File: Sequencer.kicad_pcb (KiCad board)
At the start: 2 copper layers, 100.6 x 100 mm, 230 parts, among them J1 Conn_02x03_Odd_Even, J2 Conn_02x05_Odd_Even, J3 Conn_02x03_Odd_Even, J4 Conn_01x03, Q1 BC847, Q2 BC847, Q3 BC847, Q4 BC847, SW1 SW_Push, SW10 SW_SPDT_MSM, SW11 SW_SPDT_MSM, SW12 SW_SPDT_MSM, SW2 SW_SPDT_MSM, SW3 SW_SPDT_MSM, SW4 SW_SPDT_MSM, SW5 SW_SPDT_MSM, SW6 SW_SPDT_MSM, SW7 SW_SPDT, SW8 SW_SPDT, SW9 SW_SPDT_MSM, U1 L7805, U10 TL072, U11 74AHCT1G125, U12 TL072, U13 74AHCT1G125, U14 TL072, U2 ATmega328PB-AU, U3 74AHCT1G125, U4 MCP6002-xMS, U5 MCP6002-xMS, U6 MCP6002-xMS, U7 MCP6002-xMS, U8 TL072, U9 74AHCT1G125, X1 20MHz

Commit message: Power section placement.
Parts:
- moved D3 82.6 mm to (107.9, 76.3), turned to 180 degrees
- moved R3 79.5 mm to (107.7, 79.6), turned to 180 degrees
- moved C5 41.2 mm to (128.2, 76.8)
- moved R15 28.4 mm to (158.9, 82.1), turned to 180 degrees
- moved C3 26.4 mm to (158.9, 72.2), turned to 0 degrees
- moved C4 24.6 mm to (158.9, 76.8), turned to 0 degrees
- moved C1 21.9 mm to (168.8, 76.8)
- moved U1 20.6 mm to (148.5, 74.5)
- moved D8 16.7 mm to (162.7, 59.0)
- moved C7 14.4 mm to (154.6, 120.2), turned to 0 degrees
- moved R13 12.9 mm to (158.9, 67.7)
- moved C2 12.6 mm to (189.1, 76.8)
- moved R14 11.8 mm to (158.9, 63.1)
- moved R4 10.4 mm to (142.1, 120.0), turned to 0 degrees
- moved R19 8.19 mm to (133.3, 114.4)
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
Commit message: PWM pin swap.
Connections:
- C1 pad 2: (no net) -> GND
- C10 pad 2: (no net) -> GND
- C12 pad 2: (no net) -> GND
- C13 pad 2: (no net) -> GND
- C15 pad 2: (no net) -> GND
- C16 pad 2: (no net) -> GND
- C18 pad 2: (no net) -> GND
- C19 pad 2: (no net) -> GND
- C2 pad 1: (no net) -> GND
- C21 pad 2: (no net) -> GND
- C22 pad 1: (no net) -> GND
- C23 pad 2: (no net) -> GND
- C24 pad 2: (no net) -> GND
- C25 pad 2: (no net) -> GND
- C26 pad 2: (no net) -> GND
- C29 pad 2: (no net) -> GND
- C3 pad 2: (no net) -> GND
- C30 pad 1: (no net) -> GND
- C31 pad 2: (no net) -> GND
- C32 pad 2: (no net) -> GND
- C33 pad 2: (no net) -> GND
- C34 pad 2: (no net) -> GND
- C37 pad 2: (no net) -> GND
- C38 pad 1: (no net) -> GND
- C39 pad 2: (no net) -> GND
- C4 pad 2: (no net) -> GND
- C40 pad 2: (no net) -> GND
- C41 pad 2: (no net) -> GND
- C42 pad 2: (no net) -> GND
- C45 pad 2: (no net) -> GND
- C46 pad 1: (no net) -> GND
- C47 pad 2: (no net) -> GND
- C48 pad 2: (no net) -> GND
- C49 pad 2: (no net) -> GND
- C5 pad 2: (no net) -> GND
- C50 pad 2: (no net) -> GND
- C6 pad 1: (no net) -> GND
- C7 pad 2: (no net) -> GND
- C8 pad 1: (no net) -> GND
- C9 pad 2: (no net) -> GND
- D13 pad 1: (no net) -> GND
- D14 pad 1: (no net) -> GND
- D15 pad 1: (no net) -> GND
- D3 pad 1: (no net) -> GND
- D4 pad 1: (no net) -> GND
- D5 pad 1: (no net) -> GND
- J-Inv1 pad S: (no net) -> GND
- J-Inv10 pad S: (no net) -> GND
- J-Inv11 pad S: (no net) -> GND
- J-Inv12 pad S: (no net) -> GND
- J-Inv13 pad S: (no net) -> GND
- J-Inv14 pad S: (no net) -> GND
- J-Inv15 pad S: (no net) -> GND
- J-Inv16 pad S: (no net) -> GND
- J-Inv2 pad S: (no net) -> GND
- J-Inv2 pad TN: (no net) -> GND
- J-Inv3 pad S: (no net) -> GND
- J-Inv4 pad S: (no net) -> GND
- J-Inv5 pad S: (no net) -> GND
- J-Inv5 pad TN: (no net) -> GND
- J-Inv6 pad S: (no net) -> GND
- J-Inv7 pad S: (no net) -> GND
- J-Inv8 pad S: (no net) -> GND
- J-Inv9 pad S: (no net) -> GND
- J1 pad 1: (no net) -> GND
- J1 pad 2: (no net) -> GND
- J2 pad 3: (no net) -> GND
- J2 pad 4: (no net) -> GND
- J2 pad 5: (no net) -> GND
- J2 pad 6: (no net) -> GND
- J2 pad 7: (no net) -> GND
- J2 pad 8: (no net) -> GND
- J3 pad 6: (no net) -> GND
- J4 pad 1: (no net) -> GND
- J4 pad 3: CV3 -> CV0
- Q1 pad 2: (no net) -> GND
- Q2 pad 2: (no net) -> GND
- Q3 pad 2: (no net) -> GND
- Q4 pad 2: (no net) -> GND
- R101 pad 2: (no net) -> GND
- R103 pad 2: (no net) -> GND
- R105 pad 1: (no net) -> GND
- R107 pad 2: (no net) -> GND
- R11 pad 2: (no net) -> GND
- R19 pad 2: (no net) -> GND
- R24 pad 2: (no net) -> GND
- R29 pad 2: (no net) -> GND
- R44 pad 1: (no net) -> GND
- R47 pad 2: (no net) -> GND
- R49 pad 2: (no net) -> GND
- R51 pad 1: (no net) -> GND
- R53 pad 2: (no net) -> GND
- R62 pad 1: (no net) -> GND
- R65 pad 2: (no net) -> GND
- R67 pad 2: (no net) -> GND
- R69 pad 1: (no net) -> GND
- R71 pad 2: (no net) -> GND
- R80 pad 1: (no net) -> GND
- R83 pad 2: (no net) -> GND
- R85 pad 2: (no net) -> GND
- R87 pad 1: (no net) -> GND
- R89 pad 2: (no net) -> GND
- R98 pad 1: (no net) -> GND
- RV1 pad 3: (no net) -> GND
- RV2 pad 3: (no net) -> GND
- RV3 pad 3: (no net) -> GND
- RV4 pad 3: (no net) -> GND
- SW1 pad 2: (no net) -> GND
- U1 pad 2: (no net) -> GND
- U11 pad 1: (no net) -> GND
- U11 pad 3: (no net) -> GND
- U13 pad 1: (no net) -> GND
- U13 pad 3: (no net) -> GND
- U2 pad 13: CV0 -> CV2
- U2 pad 14: CV1 -> CV3
- U2 pad 21: (no net) -> GND
- U2 pad 30: CV3 -> CV0
- U2 pad 32: CV2 -> CV1
- U2 pad 5: (no net) -> GND
- U3 pad 1: (no net) -> GND
- U3 pad 3: (no net) -> GND
- U4 pad 4: (no net) -> GND
- U5 pad 4: (no net) -> GND
- U6 pad 4: (no net) -> GND
- U7 pad 4: (no net) -> GND
- U9 pad 1: (no net) -> GND
- U9 pad 3: (no net) -> GND
- X1 pad 2: (no net) -> GND

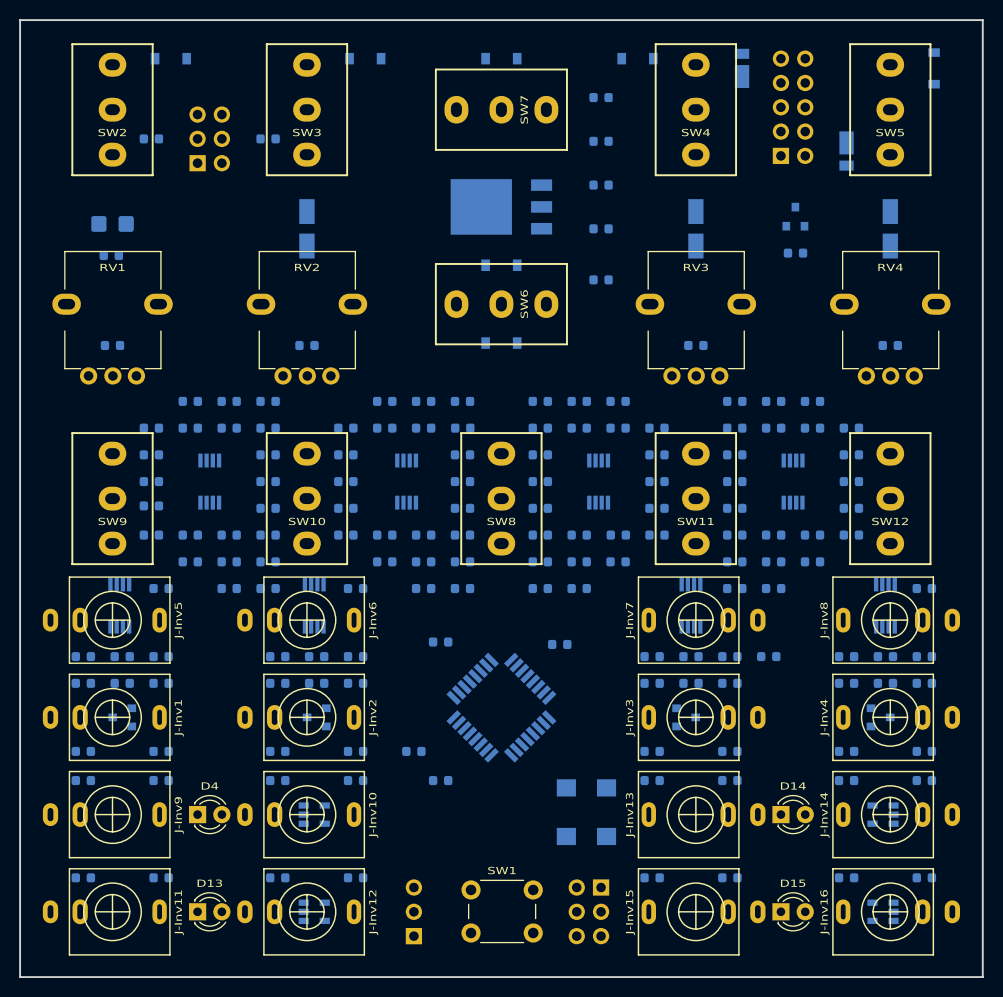
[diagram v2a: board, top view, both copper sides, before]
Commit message: Handrouted power and I2C.
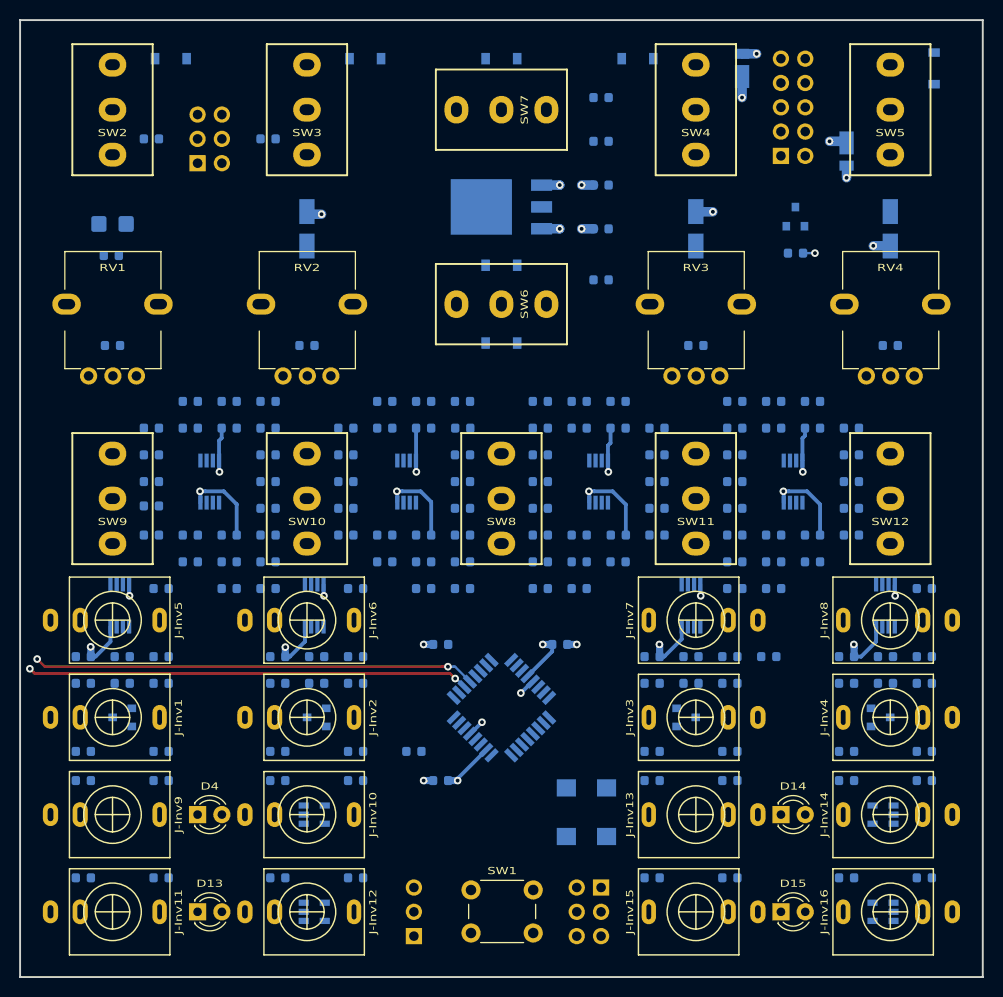
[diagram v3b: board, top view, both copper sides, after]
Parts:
- moved R4 0.25 mm to (142.1, 120.2)
- turned C22 to 180 degrees
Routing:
- net +12V: track 0.00 -> 220.4 mm, vias 0 -> 8
- net +5V: track 0.00 -> 193.6 mm, vias 0 -> 10
- net -12V: track 0.00 -> 139.1 mm, vias 0 -> 7
- net SCL: track 0.00 -> 119.6 mm, vias 0 -> 2
- net SDA: track 0.00 -> 112.9 mm, vias 0 -> 2
- net GND: track 0.00 -> 10.3 mm, vias 0 -> 8
- net Net-(D2-Pad1): track 0.00 -> 7.56 mm, vias 0 -> 1
- net Net-(D1-Pad2): track 0.00 -> 6.81 mm, vias 0 -> 1
- added copper zone on In2.Cu, net +5V
- added copper zone on In1.Cu, net GND
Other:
- copper layers 2 -> 4

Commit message: Autorouted remaining traces.
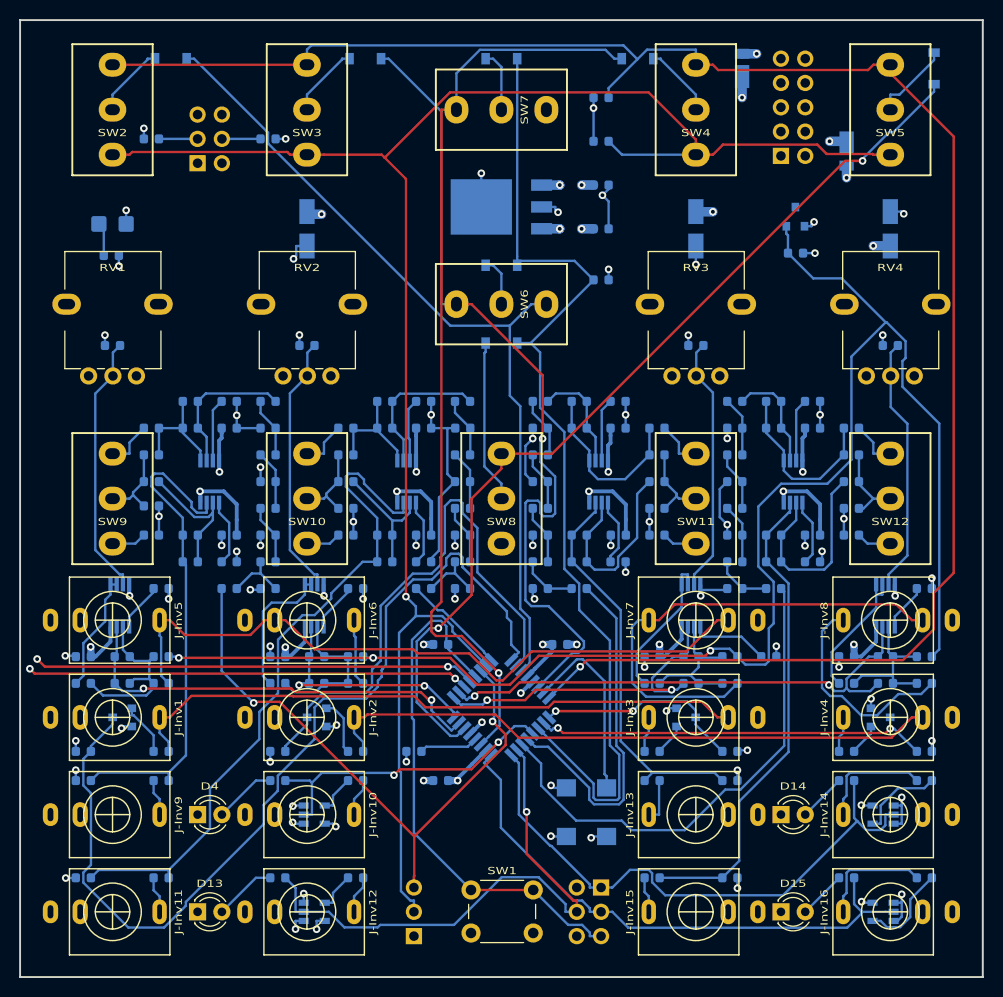
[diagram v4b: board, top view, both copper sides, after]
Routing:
- net Sense1: track 0.00 -> 197.5 mm, vias 0 -> 1
- net Sense0: track 0.00 -> 190.2 mm, vias 0 -> 1
- net VRef-10: track 0.00 -> 166.0 mm, vias 0 -> 3
- net GND: track 10.3 -> 143.3 mm, vias 8 -> 69
- net Sense2: track 0.00 -> 105.0 mm
- net CLK0: track 0.00 -> 99.7 mm
- net Scan3: track 0.00 -> 98.7 mm, vias 0 -> 2
- net Scan2: track 0.00 -> 96.2 mm, vias 0 -> 1
- net Scan0: track 0.00 -> 88.0 mm
- net Scan1: track 0.00 -> 87.3 mm, vias 0 -> 1
- net /CVIn/In: track 0.00 -> 73.0 mm
- net Net-(C36-Pad1): track 0.00 -> 71.5 mm
- net /DigitalIn/In: track 0.00 -> 65.7 mm
- net /sheet5C188821/In: track 0.00 -> 65.4 mm
- net CV0: track 0.00 -> 63.8 mm, vias 0 -> 2
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
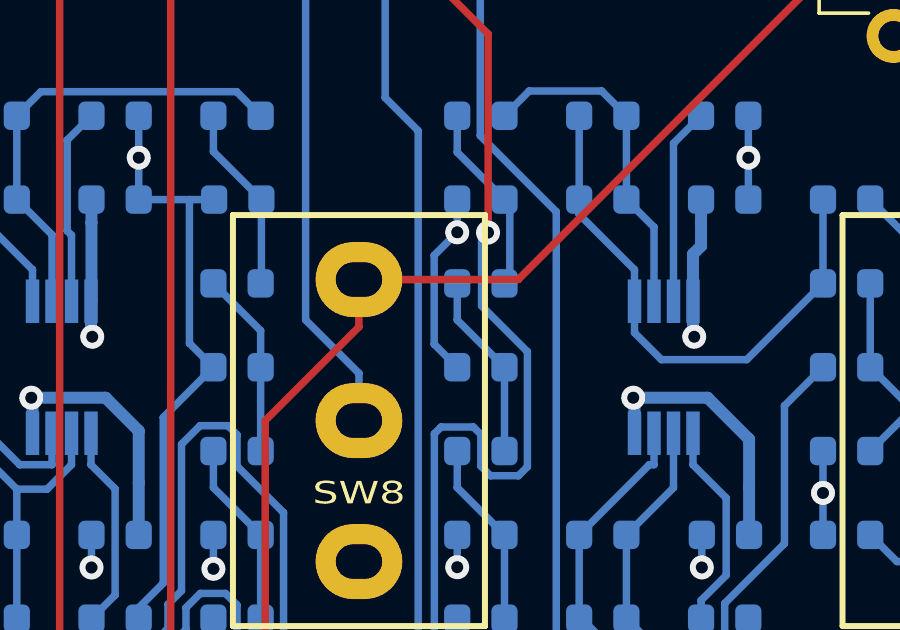
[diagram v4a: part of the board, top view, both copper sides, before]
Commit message: Corrected one single DRC (unconnected).
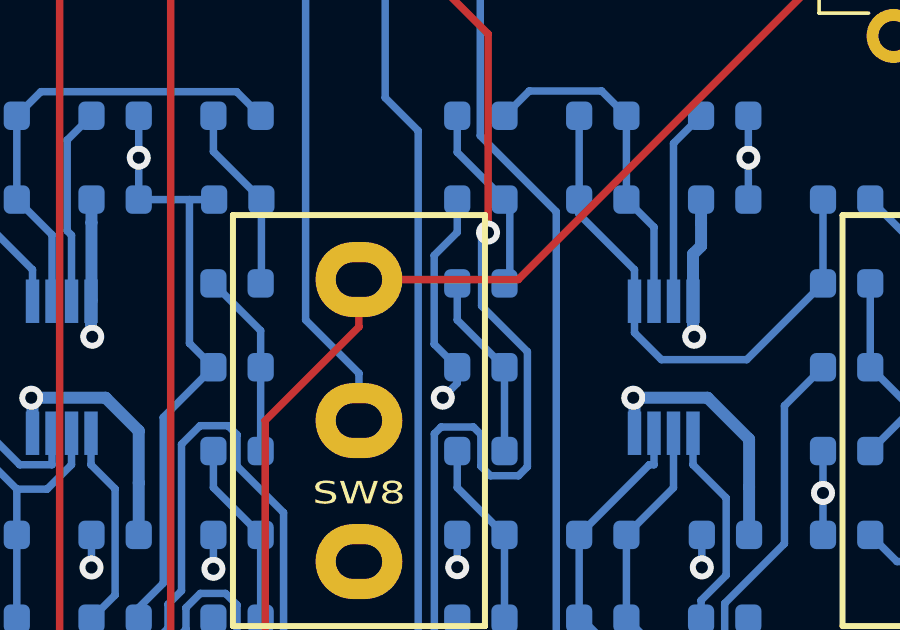
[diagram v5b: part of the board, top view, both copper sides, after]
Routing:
- net GND: track 143.3 -> 144.6 mm
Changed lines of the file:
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@@
     (thickness 1.6)
     (drawings 88)
-    (tracks 1616)
+    (tracks 1618)
     (zones 0)
     (modules 230)
@@
   (via (at 127.3915 87.9081) (size 0.8) (layers F.Cu B.Cu) (net 149))
   (via (at 180.2235 109.9382) (size 0.8) (layers F.Cu B.Cu) (net 149))
-  (via (at 151.7755 98.7333) (size 0.8) (layers F.Cu B.Cu) (net 149))
   (via (at 159.0573 73.3048) (size 0.8) (layers F.Cu B.Cu) (net 149))
   (via (at 188.3515 87.9218) (size 0.8) (layers F.Cu B.Cu) (net 149))
@@
   (via (at 169.327 115.169) (size 0.8) (layers F.Cu B.Cu) (net 149))
   (via (at 129.957 115.169) (size 0.8) (layers F.Cu B.Cu) (net 149))
+  (segment (start 151.7755 103.231) (end 151.7755 103.76374) (width 0.25) (layer B.Cu) (net 149))
+  (via (at 151.29256 104.24668) (size 0.8) (drill 0.4) (layers F.Cu B.Cu) (net 149))
+  (segment (start 151.7755 103.76374) (end 151.29256 104.24668) (width 0.25) (layer B.Cu) (net 149))
   (zone (net 3) (net_name +5V) (layer In2.Cu) (hatch edge 0.508)
     (connect_pads (clearance 0.762))

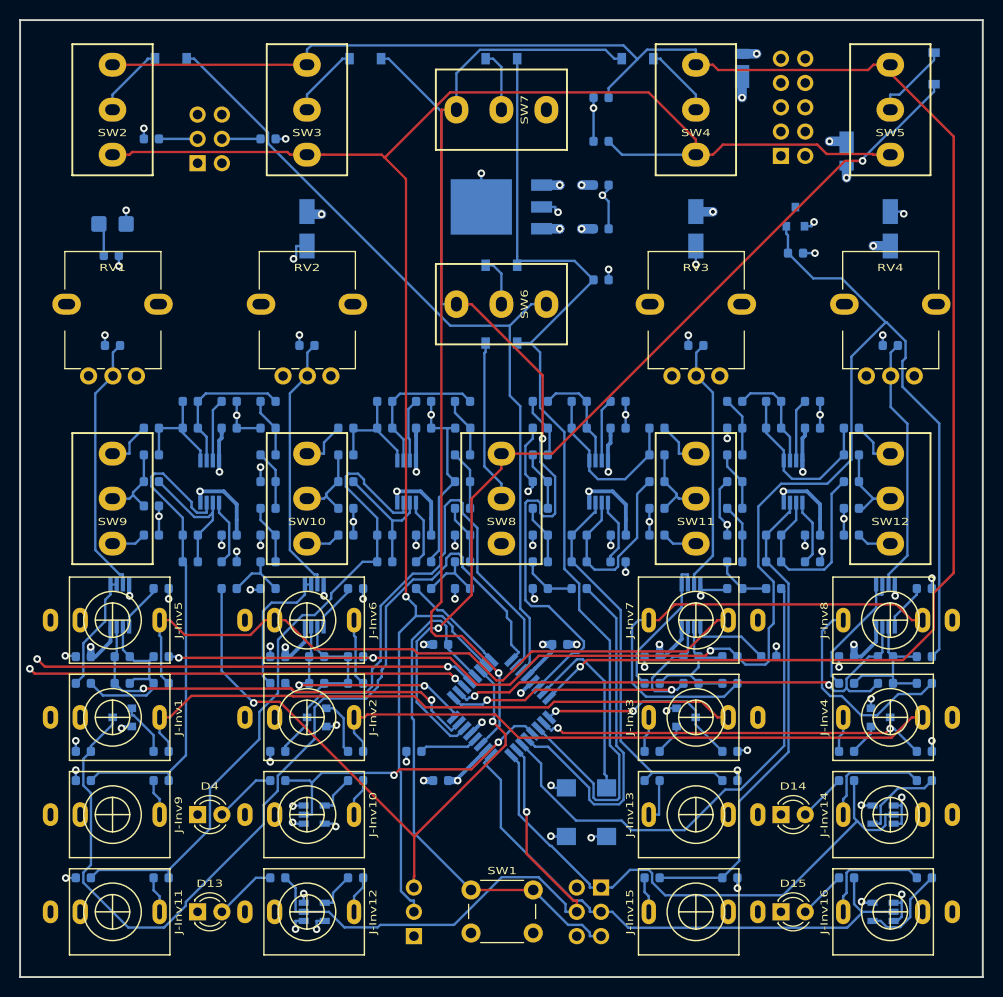
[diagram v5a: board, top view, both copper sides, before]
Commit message: Fixed clearances on front copper.
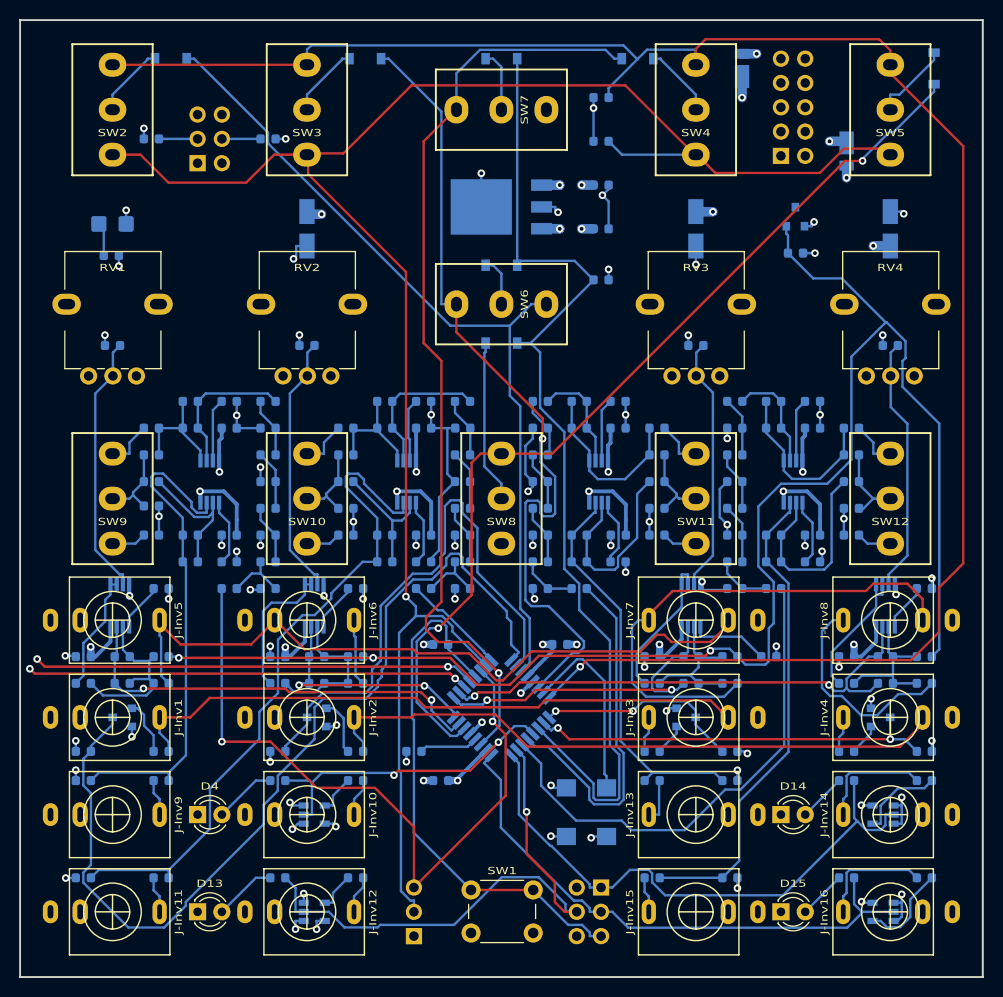
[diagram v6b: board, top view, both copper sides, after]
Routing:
- net CV0: track 63.8 -> 73.9 mm
- net Sense0: track 190.2 -> 196.8 mm
- net Sense1: track 197.5 -> 203.3 mm
- net /sheet5C1536C4/In: track 50.1 -> 53.5 mm
- net /CVIn/In: track 73.0 -> 74.9 mm
- net Scan2: track 96.2 -> 97.5 mm
- net Scan3: track 98.7 -> 100.0 mm
- net /sheet5C188821/In: track 65.4 -> 66.5 mm
- net Scan1: track 87.3 -> 86.4 mm
- net GND: track 144.6 -> 145.3 mm
- net RST1: track 42.0 -> 42.7 mm
- net TRIG1: track 57.9 -> 58.5 mm
